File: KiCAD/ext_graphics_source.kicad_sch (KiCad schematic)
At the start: 19 parts, among them J2 Conn_01x20, J3 Conn_01x20, J4 Conn_01x20, J5 Conn_01x20, U32 74AHC595, U33 74AHC595, U34 74AHC595

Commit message: finished schematics and footprint assignments; need to figure out +5v connection issue
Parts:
- J2, J3, J4, J5: footprint Connector_PinHeader_2.54mm:PinHeader_1x20_P2.54mm_Vertical -> Connector_PinSocket_2.54mm:PinSocket_1x20_P2.54mm_Vertical
- R10, R11, R12, R13, R2, R3, R4, R5, R6, R7, R8, R9: footprint (none) -> Resistor_THT:R_Axial_DIN0207_L6.3mm_D2.5mm_P7.62mm_Horizontal
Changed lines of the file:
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@@
 			)
 		)
-		(property "Footprint" ""
+		(property "Footprint" "Resistor_THT:R_Axial_DIN0207_L6.3mm_D2.5mm_P7.62mm_Horizontal"
 			(at 70.358 53.34 90)
 			(effects
@@
 			)
 		)
-		(property "Footprint" ""
+		(property "Footprint" "Resistor_THT:R_Axial_DIN0207_L6.3mm_D2.5mm_P7.62mm_Horizontal"
 			(at 47.498 53.34 90)
 			(effects
@@
 			)
 		)
-		(property "Footprint" ""
+		(property "Footprint" "Resistor_THT:R_Axial_DIN0207_L6.3mm_D2.5mm_P7.62mm_Horizontal"
 			(at 47.498 154.94 90)
 			(effects
@@
 			)
 		)
-		(property "Footprint" "Connector_PinHeader_2.54mm:PinHeader_1x20_P2.54mm_Vertical"
+		(property "Footprint" "Connector_PinSocket_2.54mm:PinSocket_1x20_P2.54mm_Vertical"
 			(at 195.58 92.71 0)
 			(effects
@@
 			)
 		)
-		(property "Footprint" ""
+		(property "Footprint" "Resistor_THT:R_Axial_DIN0207_L6.3mm_D2.5mm_P7.62mm_Horizontal"
 			(at 62.738 154.94 90)
 			(effects
@@
 			)
 		)
-		(property "Footprint" ""
+		(property "Footprint" "Resistor_THT:R_Axial_DIN0207_L6.3mm_D2.5mm_P7.62mm_Horizontal"
 			(at 70.358 154.94 90)
 			(effects
@@
 			)
 		)
-		(property "Footprint" "Connector_PinHeader_2.54mm:PinHeader_1x20_P2.54mm_Vertical"
+		(property "Footprint" "Connector_PinSocket_2.54mm:PinSocket_1x20_P2.54mm_Vertical"
 			(at 147.32 92.71 0)
 			(effects
@@
 			)
 		)
-		(property "Footprint" "Connector_PinHeader_2.54mm:PinHeader_1x20_P2.54mm_Vertical"
+		(property "Footprint" "Connector_PinSocket_2.54mm:PinSocket_1x20_P2.54mm_Vertical"
 			(at 167.64 92.71 0)
 			(effects
@@
 			)
 		)
-		(property "Footprint" ""
+		(property "Footprint" "Resistor_THT:R_Axial_DIN0207_L6.3mm_D2.5mm_P7.62mm_Horizontal"
 			(at 55.118 104.14 90)
 			(effects
@@
 			)
 		)
-		(property "Footprint" ""
+		(property "Footprint" "Resistor_THT:R_Axial_DIN0207_L6.3mm_D2.5mm_P7.62mm_Horizontal"
 			(at 70.358 104.14 90)
 			(effects
@@
 			)
 		)
-		(property "Footprint" "Connector_PinHeader_2.54mm:PinHeader_1x20_P2.54mm_Vertical"
+		(property "Footprint" "Connector_PinSocket_2.54mm:PinSocket_1x20_P2.54mm_Vertical"
 			(at 220.98 92.71 0)
 			(effects
@@
 			)
 		)
-		(property "Footprint" ""
+		(property "Footprint" "Resistor_THT:R_Axial_DIN0207_L6.3mm_D2.5mm_P7.62mm_Horizontal"
 			(at 55.118 154.94 90)
 			(effects
@@
 			)
 		)
-		(property "Footprint" ""
+		(property "Footprint" "Resistor_THT:R_Axial_DIN0207_L6.3mm_D2.5mm_P7.62mm_Horizontal"
 			(at 62.738 53.34 90)
 			(effects
@@
 			)
 		)
-		(property "Footprint" ""
+		(property "Footprint" "Resistor_THT:R_Axial_DIN0207_L6.3mm_D2.5mm_P7.62mm_Horizontal"
 			(at 62.738 104.14 90)
 			(effects
@@
 			)
 		)
-		(property "Footprint" ""
+		(property "Footprint" "Resistor_THT:R_Axial_DIN0207_L6.3mm_D2.5mm_P7.62mm_Horizontal"
 			(at 47.498 104.14 90)
 			(effects
@@
 			)
 		)
-		(property "Footprint" ""
+		(property "Footprint" "Resistor_THT:R_Axial_DIN0207_L6.3mm_D2.5mm_P7.62mm_Horizontal"
 			(at 55.118 53.34 90)
 			(effects

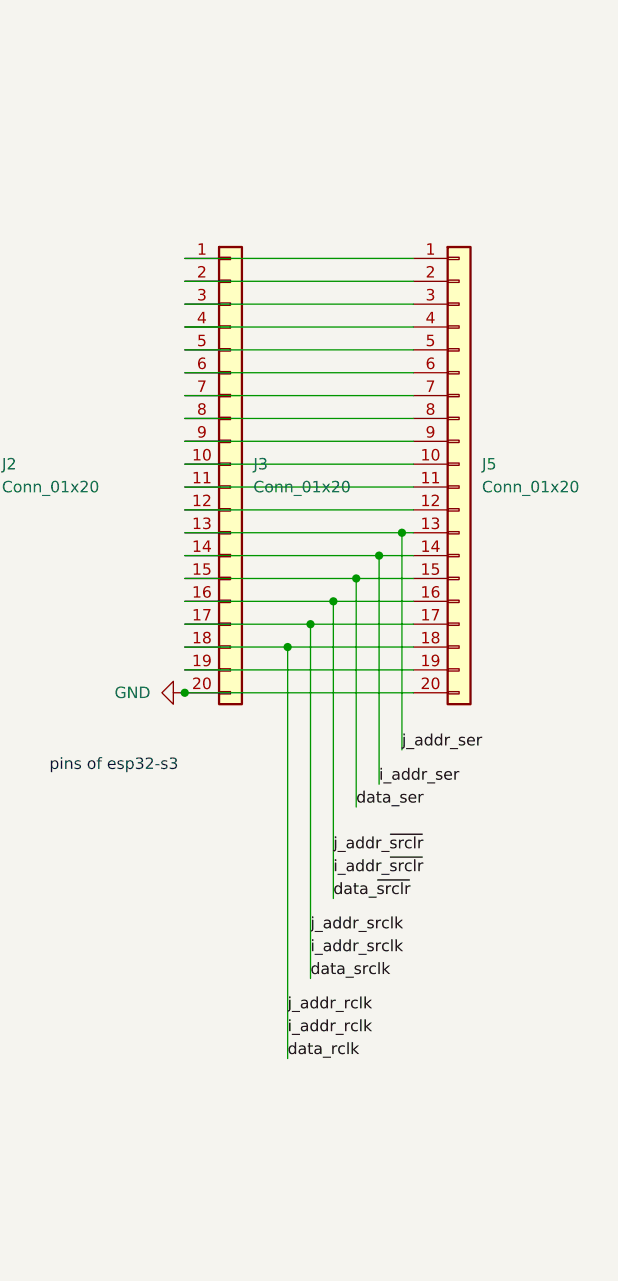
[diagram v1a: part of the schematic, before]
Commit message: modified debug connector; changed board type in pcb editor
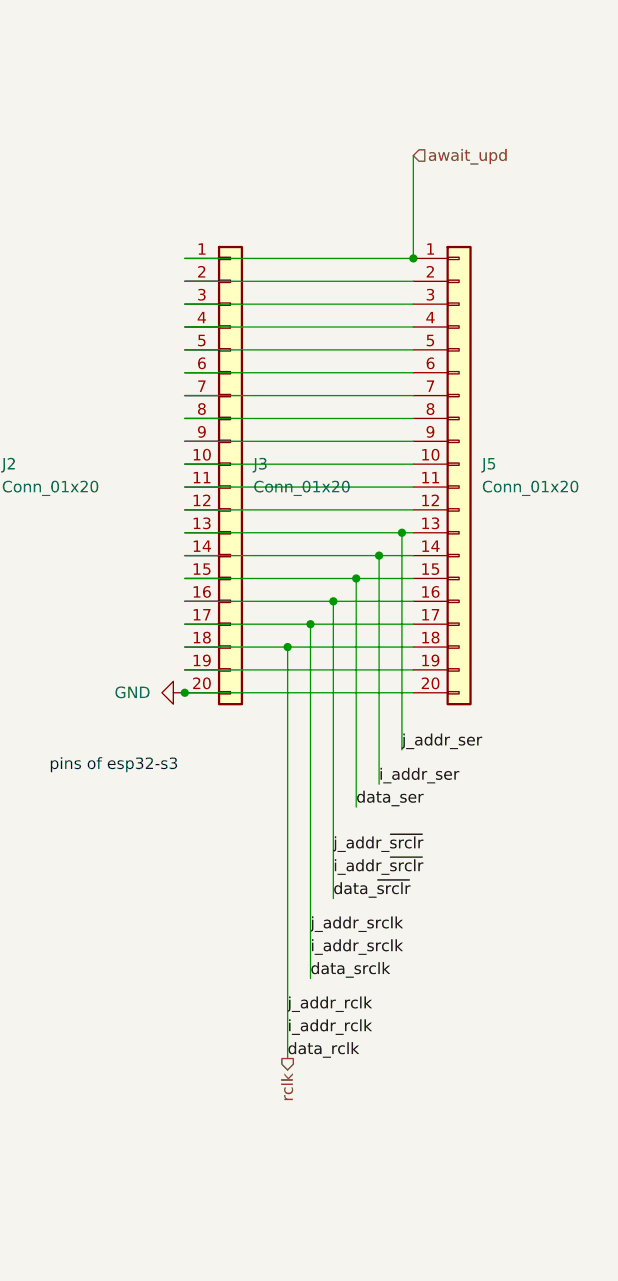
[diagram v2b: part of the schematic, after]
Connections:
- net await_upd: now reaches J3.1 (Pin_1), J5.1 (Pin_1)
- net data_rclk renamed rclk
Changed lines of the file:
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@@
+	)
+	(junction
+		(at 215.9 69.85)
+		(diameter 0)
+		(color 0 0 0 0)
 	)
 	(junction
@@
 	(wire
 		(pts
+			(xy 215.9 58.42) (xy 215.9 69.85)
+		)
+		(stroke
+			(width 0)
+			(type default)
+		)
+	)
+	(wire
+		(pts
 			(xy 190.5 95.25) (xy 215.9 95.25)
 		)
@@
 			)
 			(justify left bottom)
+		)
+	)
+	(hierarchical_label "rclk"
+		(shape output)
+		(at 201.93 158.75 270)
+		(effects
+			(font
+				(size 1.27 1.27)
+			)
+			(justify right)
 		)
 	)
@@
 		(effects
 			(font
+				(size 1.27 1.27)
+			)
+			(justify left)
+		)
+	)
+	(hierarchical_label "await_upd"
+		(shape input)
+		(at 215.9 58.42 0)
+		(effects
+			(font

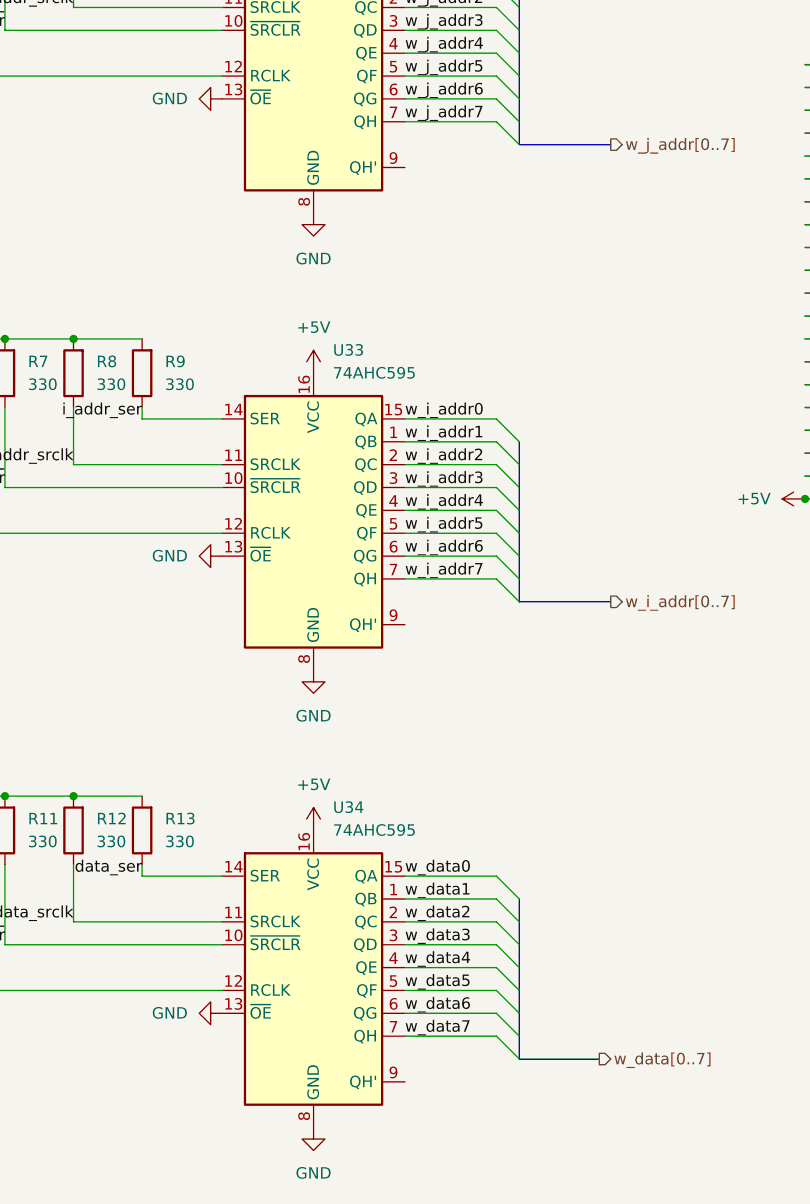
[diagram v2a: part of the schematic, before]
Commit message: fix multiple ERCs that made RAM addrs not connecting
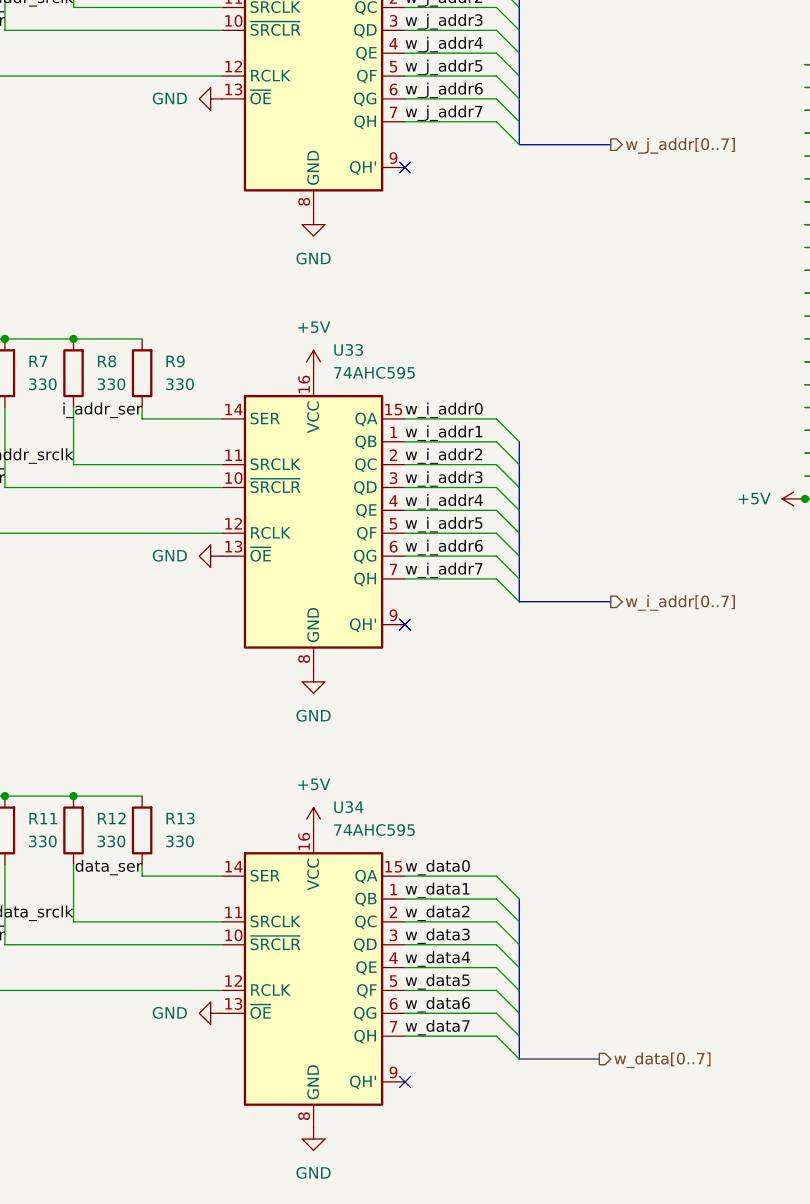
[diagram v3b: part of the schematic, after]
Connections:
- no-connect marks 0 -> 3
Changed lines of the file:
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@@
 		(color 0 0 0 0)
+	)
+	(no_connect
+		(at 97.79 81.28)
+	)
+	(no_connect
+		(at 97.79 182.88)
+	)
+	(no_connect
+		(at 97.79 132.08)
 	)
 	(bus_entry

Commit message: resolve ERCs for addr combiner
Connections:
- net w_data0 renamed data0
- net w_data1 renamed data1
- net w_data2 renamed data2
- net w_data3 renamed data3
- net w_data4 renamed data4
- net w_data5 renamed data5
- net w_data6 renamed data6
- net w_data7 renamed data7
- net w_i_addr0 renamed i_addr0
- net w_i_addr1 renamed i_addr1
- net w_i_addr2 renamed i_addr2
- net w_i_addr3 renamed i_addr3
- net w_i_addr4 renamed i_addr4
- net w_i_addr5 renamed i_addr5
- net w_i_addr6 renamed i_addr6
- net w_i_addr7 renamed i_addr7
- net w_j_addr0 renamed j_addr0
- net w_j_addr1 renamed j_addr1
- net w_j_addr2 renamed j_addr2
- net w_j_addr3 renamed j_addr3
- net w_j_addr4 renamed j_addr4
- net w_j_addr5 renamed j_addr5
- net w_j_addr6 renamed j_addr6
- net w_j_addr7 renamed j_addr7
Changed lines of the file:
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@@
 		)
 	)
-	(label "w_j_addr1"
+	(label "j_addr1"
 		(at 97.79 60.96 0)
 		(effects
@@
 		)
 	)
-	(label "w_data3"
-		(at 97.79 167.64 0)
-		(effects
-			(font
-				(size 1.27 1.27)
-			)
-			(justify left bottom)
-		)
-	)
 	(label "j_addr_srclk"
 		(at 204.47 144.78 0)
@@
 		)
 	)
-	(label "w_j_addr5"
+	(label "j_addr5"
 		(at 97.79 71.12 0)
 		(effects
@@
 		)
 	)
-	(label "w_data5"
-		(at 97.79 172.72 0)
-		(effects
-			(font
-				(size 1.27 1.27)
-			)
-			(justify left bottom)
-		)
-	)
-	(label "w_data1"
-		(at 97.79 162.56 0)
-		(effects
-			(font
-				(size 1.27 1.27)
-			)
-			(justify left bottom)
-		)
-	)
-	(label "w_data0"
-		(at 97.79 160.02 0)
-		(effects
-			(font
-				(size 1.27 1.27)
-			)
-			(justify left bottom)
-		)
-	)
-	(label "w_i_addr4"
+	(label "i_addr4"
 		(at 97.79 119.38 0)
 		(effects
@@
 		)
 	)
-	(label "w_j_addr4"
+	(label "data1"
+		(at 99.06 162.56 0)
+		(effects
+			(font
+				(size 1.27 1.27)
+			)
+			(justify left bottom)
+		)
+	)
+	(label "j_addr4"
 		(at 97.79 68.58 0)
 		(effects
@@
 		)
 	)
-	(label "w_data7"
-		(at 97.79 177.8 0)
-		(effects
-			(font
-				(size 1.27 1.27)
-			)
-			(justify left bottom)
-		)
-	)
-	(label "w_j_addr2"
+	(label "j_addr2"
 		(at 97.79 63.5 0)
 		(effects
@@
 		)
 	)
-	(label "w_j_addr0"
+	(label "j_addr0"
 		(at 97.79 58.42 0)
-		(effects
-			(font
-				(size 1.27 1.27)
-			)
-			(justify left bottom)
-		)
-	)
-	(label "w_data2"
-		(at 97.79 165.1 0)
 		(effects
 			(font
@@
 		)
 	)
-	(label "w_i_addr1"
+	(label "i_addr1"
 		(at 97.79 111.76 0)
 		(effects
@@
 		)
 	)
-	(label "w_data4"
-		(at 97.79 170.18 0)
-		(effects
-			(font
-				(size 1.27 1.27)
-			)
-			(justify left bottom)
-		)
-	)
-	(label "w_i_addr5"
+	(label "i_addr5"
 		(at 97.79 121.92 0)
+		(effects
+			(font
+				(size 1.27 1.27)
+			)
+			(justify left bottom)
+		)
+	)
+	(label "data0"
+		(at 99.06 160.02 0)
 		(effects
 			(font
@@
 		)
 	)
-	(label "w_i_addr7"
+	(label "i_addr7"
 		(at 97.79 127 0)
+		(effects
+			(font
+				(size 1.27 1.27)
+			)
+			(justify left bottom)
+		)
+	)
+	(label "data5"
+		(at 99.06 172.72 0)
 		(effects
 			(font
@@
 		)
 	)
-	(label "w_i_addr6"
+	(label "data6"
+		(at 99.06 175.26 0)
+		(effects
+			(font
+				(size 1.27 1.27)
+			)
+			(justify left bottom)
+		)
+	)
+	(label "i_addr6"
 		(at 97.79 124.46 0)
 		(effects
@@
 		)
 	)
+	(label "data7"
+		(at 99.06 177.8 0)
+		(effects
+			(font
+				(size 1.27 1.27)
+			)
+			(justify left bottom)
+		)
+	)
+	(label "data3"
+		(at 99.06 167.64 0)
+		(effects
+			(font
+				(size 1.27 1.27)
+			)
+			(justify left bottom)
+		)
+	)
 	(label "j_addr_rclk"
 		(at 45.72 71.12 180)
@@
 		)
 	)
-	(label "w_i_addr3"
+	(label "i_addr3"
 		(at 97.79 116.84 0)
-		(effects
-			(font
-				(size 1.27 1.27)
-			)
-			(justify left bottom)
-		)
-	)
-	(label "w_data6"
-		(at 97.79 175.26 0)
 		(effects
 			(font
@@
 		)
 	)
-	(label "w_j_addr3"
+	(label "j_addr3"
 		(at 97.79 66.04 0)
 		(effects
@@
 		)
 	)
-	(label "w_i_addr0"
+	(label "i_addr0"
 		(at 97.79 109.22 0)
 		(effects
@@
 		)
 	)
-	(label "w_i_addr2"
+	(label "i_addr2"
 		(at 97.79 114.3 0)
 		(effects
@@
 		)
 	)
+	(label "data2"
+		(at 99.06 165.1 0)
+		(effects
+			(font
+				(size 1.27 1.27)
+			)
+			(justify left bottom)
+		)
+	)
 	(label "i_addr_~{srclr}"
 		(at 53.34 116.84 180)
@@
 		)
 	)
+	(label "data4"
+		(at 99.06 170.18 0)
+		(effects
+			(font
+				(size 1.27 1.27)
+			)
+			(justify left bottom)
+		)
+	)
 	(label "i_addr_rclk"
 		(at 201.93 156.21 0)
@@
 		)
 	)
-	(label "w_j_addr7"
+	(label "j_addr7"
 		(at 97.79 76.2 0)
 		(effects
@@
 		)
 	)
-	(label "w_j_addr6"
+	(label "j_addr6"
 		(at 97.79 73.66 0)
 		(effects
@@
 		)
 	)
-	(hierarchical_label "w_data[0..7]"
+	(hierarchical_label "data[0..7]"
 		(shape output)
 		(at 119.38 180.34 0)
@@
 		)
 	)
-	(hierarchical_label "w_i_addr[0..7]"
+	(hierarchical_label "i_addr[0..7]"
 		(shape output)
 		(at 120.65 129.54 0)
@@
 		)
 	)
-	(hierarchical_label "w_j_addr[0..7]"
+	(hierarchical_label "j_addr[0..7]"
 		(shape output)
 		(at 120.65 78.74 0)

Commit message: updated KiCAD todos
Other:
- note added: "TODO: change orientation in PCB"
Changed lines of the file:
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@@
+		)
+	)
+	(text "TODO: change orientation in PCB\n"
+		(exclude_from_sim no)
+		(at 179.578 62.23 0)
+		(effects
+			(font
+				(size 1.27 1.27)
+			)
 		)
 	)

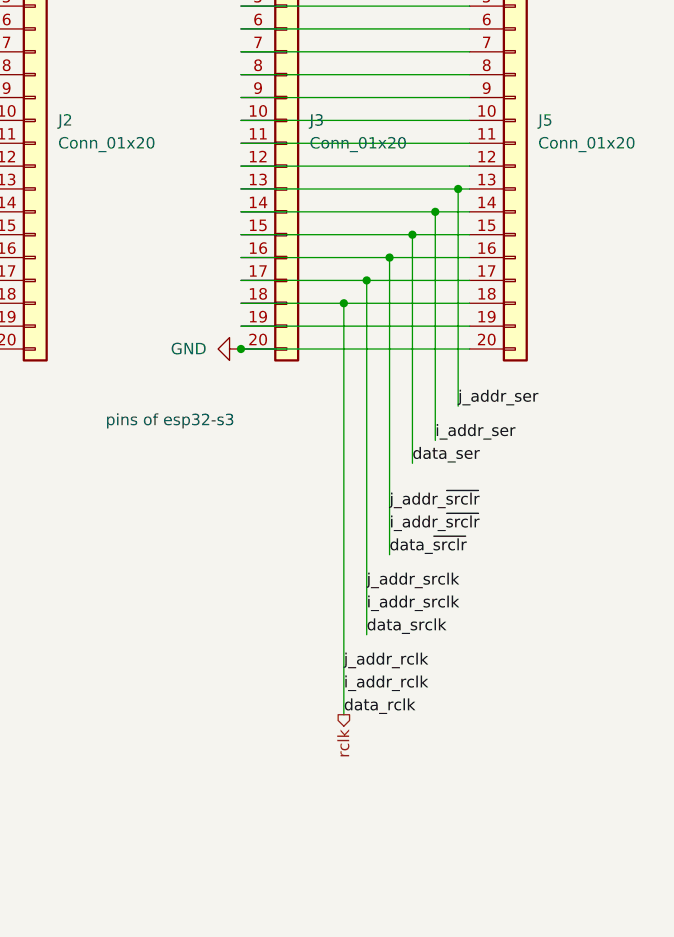
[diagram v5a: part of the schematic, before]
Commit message: update DAC schematics; update pin layout for esp32 connector; update RAM state controller input pin
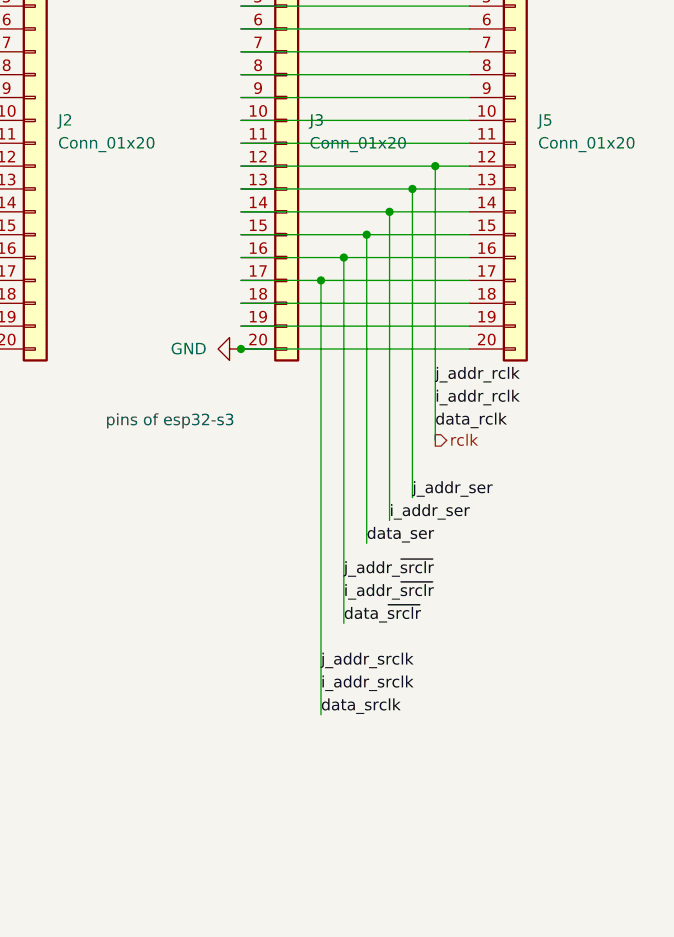
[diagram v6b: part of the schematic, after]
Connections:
- net rclk: now also J3.12 (Pin_12), J5.12 (Pin_12); no longer J3.18 (Pin_18), J5.18 (Pin_18)
- new net: J3.18 (Pin_18), J5.18 (Pin_18)

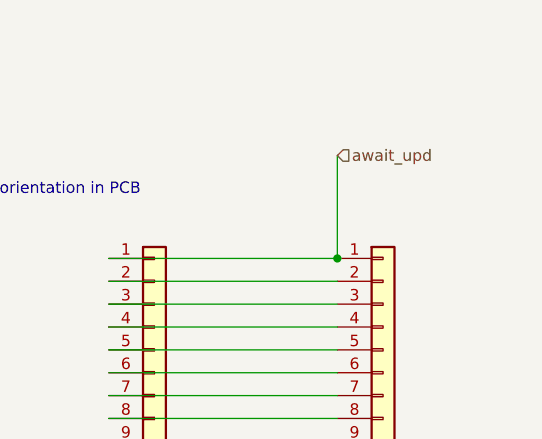
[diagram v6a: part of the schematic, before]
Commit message: passed DRC for PCB
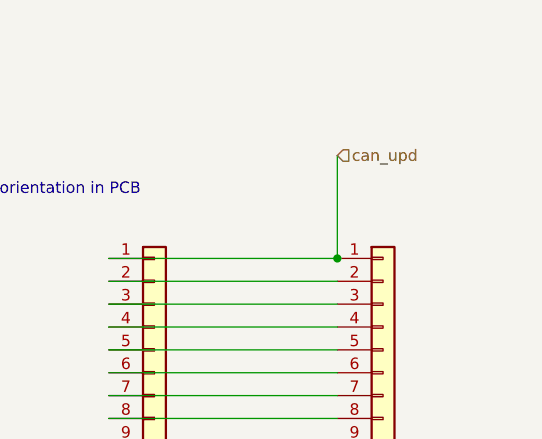
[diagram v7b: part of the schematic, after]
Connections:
- net await_upd renamed can_upd
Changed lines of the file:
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@@
 		)
 	)
-	(hierarchical_label "await_upd"
+	(hierarchical_label "can_upd"
 		(shape input)
 		(at 215.9 58.42 0)
